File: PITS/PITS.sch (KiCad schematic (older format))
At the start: 47 parts, among them P1 CONN_02X20, P10 I2C, P11 I2C, P12 I2C, P13 I2C, P14 BATT, P2 BNC, P3 BNC, P4 BNC, P5 BNC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

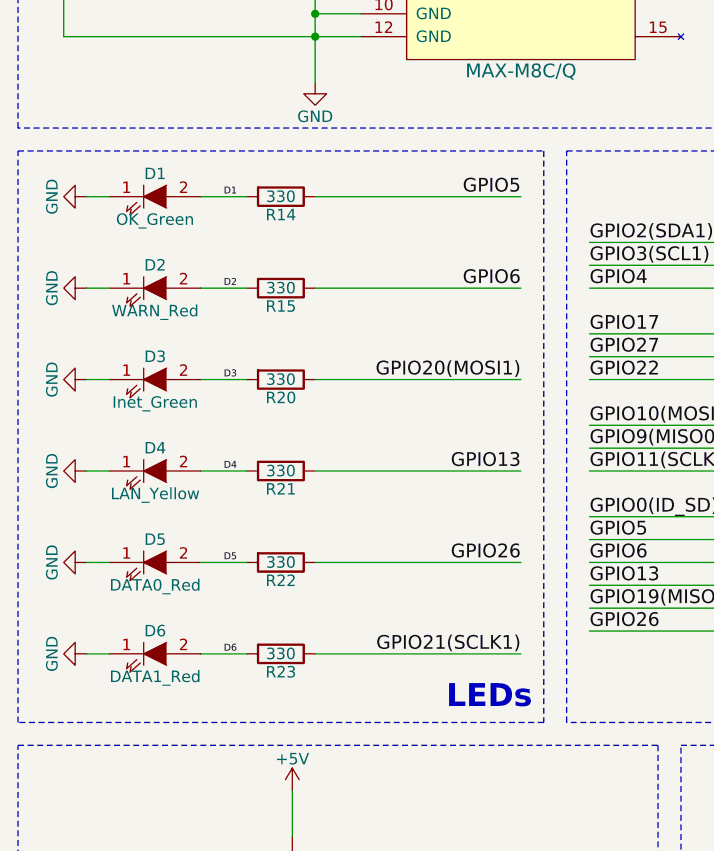
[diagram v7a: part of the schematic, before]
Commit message: layout - work in progress - first digital nets
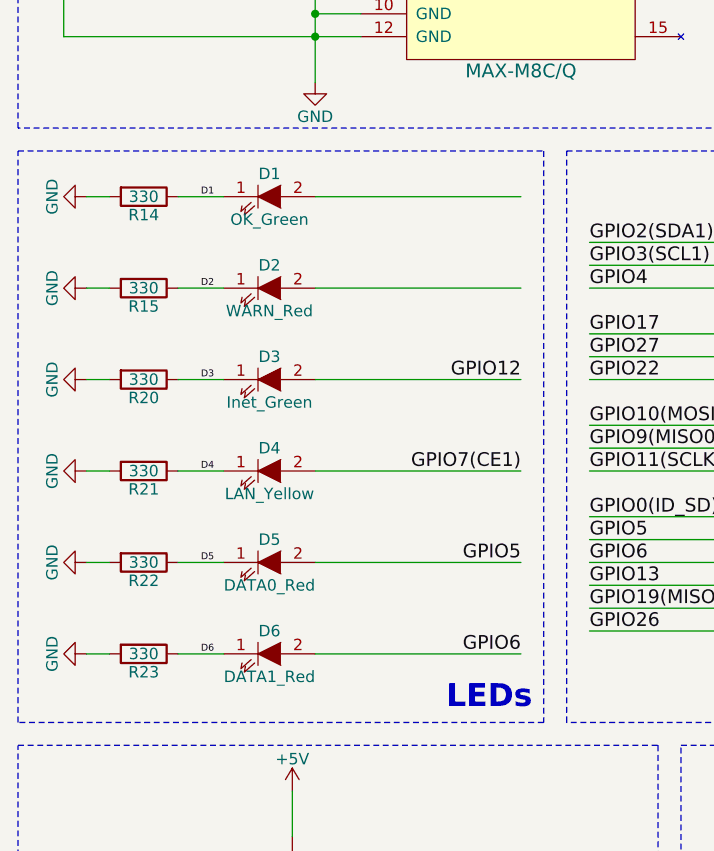
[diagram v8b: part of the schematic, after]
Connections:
- net D1: now also D1.1 (K), R14.1; no longer D1.2 (A), R14.2
- net D2: now also D2.1 (K), R15.1; no longer D2.2 (A), R15.2
- net D3: now also D3.1 (K), R20.1; no longer D3.2 (A), R20.2
- net D4: now also D4.1 (K), R21.1; no longer D4.2 (A), R21.2
- net D5: now also D5.1 (K), R22.1; no longer D5.2 (A), R22.2
- net D6: now also D6.1 (K), R23.1; no longer D6.2 (A), R23.2
- net GND: now also R14.2, R15.2, R20.2, R21.2, R22.2, R23.2; no longer D1.1 (K), D2.1 (K), D3.1 (K), D4.1 (K), D5.1 (K), D6.1 (K)
- net GPIO12: now also D3.2 (A)
- net GPIO13: no longer R21.1
- net GPIO20(MOSI1): no longer R20.1
- net GPIO21(SCLK1): no longer R23.1
- net GPIO26: no longer R22.1
- net GPIO5: now also D5.2 (A); no longer R14.1
- net GPIO6: now also D6.2 (A); no longer R15.1
- net GPIO7(CE1): now also D4.2 (A)
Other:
- moved on the sheet: D1, D2, D3, D4, D5, D6, R14, R15, R20, R21, R22, R23
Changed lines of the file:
@@
 L LED D1
 U 1 1 58198207
-P 1200 2900
-F 0 "D1" H 1200 3000 50  0000 C CNN
-F 1 "OK_Green" H 1200 2800 50  0000 C CNN
-F 2 "LEDs:LED_0603" H 1200 2900 50  0001 C CNN
-F 3 "" H 1200 2900 50  0000 C CNN
-	1    1200 2900
+P 1700 2900
+F 0 "D1" H 1700 3000 50  0000 C CNN
+F 1 "OK_Green" H 1700 2800 50  0000 C CNN
+F 2 "LEDs:LED_0603" H 1700 2900 50  0001 C CNN
+F 3 "" H 1700 2900 50  0000 C CNN
+	1    1700 2900
 	1    0    0    -1
 $EndComp
@@
 L LED D2
 U 1 1 5819820E
-P 1200 3300
-F 0 "D2" H 1200 3400 50  0000 C CNN
-F 1 "WARN_Red" H 1200 3200 50  0000 C CNN
-F 2 "LEDs:LED_0603" H 1200 3300 50  0001 C CNN
-F 3 "" H 1200 3300 50  0000 C CNN
-	1    1200 3300
+P 1700 3300
+F 0 "D2" H 1700 3400 50  0000 C CNN
+F 1 "WARN_Red" H 1700 3200 50  0000 C CNN
+F 2 "LEDs:LED_0603" H 1700 3300 50  0001 C CNN
+F 3 "" H 1700 3300 50  0000 C CNN
+	1    1700 3300
 	1    0    0    -1
 $EndComp
@@
 L LED D3
 U 1 1 58198215
-P 1200 3700
-F 0 "D3" H 1200 3800 50  0000 C CNN
-F 1 "Inet_Green" H 1200 3600 50  0000 C CNN
-F 2 "LEDs:LED_0603" H 1200 3700 50  0001 C CNN
-F 3 "" H 1200 3700 50  0000 C CNN
-	1    1200 3700
+P 1700 3700
+F 0 "D3" H 1700 3800 50  0000 C CNN
+F 1 "Inet_Green" H 1700 3600 50  0000 C CNN
+F 2 "LEDs:LED_0603" H 1700 3700 50  0001 C CNN
+F 3 "" H 1700 3700 50  0000 C CNN
+	1    1700 3700
 	1    0    0    -1
 $EndComp
@@
 L R R14
 U 1 1 581983DD
-P 1750 2900
-F 0 "R14" V 1830 2900 50  0000 C CNN
-F 1 "330" V 1750 2900 50  0000 C CNN
-F 2 "Resistors_SMD:R_0603_HandSoldering" V 1680 2900 50  0001 C CNN
-F 3 "" H 1750 2900 50  0000 C CNN
-	1    1750 2900
+P 1150 2900
+F 0 "R14" V 1230 2900 50  0000 C CNN
+F 1 "330" V 1150 2900 50  0000 C CNN
+F 2 "Resistors_SMD:R_0603_HandSoldering" V 1080 2900 50  0001 C CNN
+F 3 "" H 1150 2900 50  0000 C CNN
+	1    1150 2900
 	0    1    1    0
 $EndComp
@@
 L R R15
 U 1 1 58198843
-P 1750 3300
-F 0 "R15" V 1830 3300 50  0000 C CNN
-F 1 "330" V 1750 3300 50  0000 C CNN
-F 2 "Resistors_SMD:R_0603_HandSoldering" V 1680 3300 50  0001 C CNN
-F 3 "" H 1750 3300 50  0000 C CNN
-	1    1750 3300
+P 1150 3300
+F 0 "R15" V 1230 3300 50  0000 C CNN
+F 1 "330" V 1150 3300 50  0000 C CNN
+F 2 "Resistors_SMD:R_0603_HandSoldering" V 1080 3300 50  0001 C CNN
+F 3 "" H 1150 3300 50  0000 C CNN
+	1    1150 3300
 	0    1    1    0
 $EndComp
@@
 L R R20
 U 1 1 581988DE
-P 1750 3700
-F 0 "R20" V 1830 3700 50  0000 C CNN
-F 1 "330" V 1750 3700 50  0000 C CNN
-F 2 "Resistors_SMD:R_0603_HandSoldering" V 1680 3700 50  0001 C CNN
-F 3 "" H 1750 3700 50  0000 C CNN
-	1    1750 3700
+P 1150 3700
+F 0 "R20" V 1230 3700 50  0000 C CNN
+F 1 "330" V 1150 3700 50  0000 C CNN
+F 2 "Resistors_SMD:R_0603_HandSoldering" V 1080 3700 50  0001 C CNN
+F 3 "" H 1150 3700 50  0000 C CNN
+	1    1150 3700
 	0    1    1    0
 $EndComp
@@
 L LED D4
 U 1 1 5819A39B
-P 1200 4100
-F 0 "D4" H 1200 4200 50  0000 C CNN
-F 1 "LAN_Yellow" H 1200 4000 50  0000 C CNN
-F 2 "LEDs:LED_0603" H 1200 4100 50  0001 C CNN
-F 3 "" H 1200 4100 50  0000 C CNN
-	1    1200 4100
+P 1700 4100
+F 0 "D4" H 1700 4200 50  0000 C CNN
+F 1 "LAN_Yellow" H 1700 4000 50  0000 C CNN
+F 2 "LEDs:LED_0603" H 1700 4100 50  0001 C CNN
+F 3 "" H 1700 4100 50  0000 C CNN
+	1    1700 4100
 	1    0    0    -1
 $EndComp
@@
 L LED D5
 U 1 1 5819A3A2
-P 1200 4500
-F 0 "D5" H 1200 4600 50  0000 C CNN
-F 1 "DATA0_Red" H 1200 4400 50  0000 C CNN
-F 2 "LEDs:LED_0603" H 1200 4500 50  0001 C CNN
-F 3 "" H 1200 4500 50  0000 C CNN
-	1    1200 4500
+P 1700 4500
+F 0 "D5" H 1700 4600 50  0000 C CNN
+F 1 "DATA0_Red" H 1700 4400 50  0000 C CNN
+F 2 "LEDs:LED_0603" H 1700 4500 50  0001 C CNN
+F 3 "" H 1700 4500 50  0000 C CNN
+	1    1700 4500
 	1    0    0    -1
 $EndComp
@@
 L LED D6
 U 1 1 5819A3A9
-P 1200 4900
-F 0 "D6" H 1200 5000 50  0000 C CNN
-F 1 "DATA1_Red" H 1200 4800 50  0000 C CNN
-F 2 "LEDs:LED_0603" H 1200 4900 50  0001 C CNN
-F 3 "" H 1200 4900 50  0000 C CNN
-	1    1200 4900
+P 1700 4900
+F 0 "D6" H 1700 5000 50  0000 C CNN
+F 1 "DATA1_Red" H 1700 4800 50  0000 C CNN
+F 2 "LEDs:LED_0603" H 1700 4900 50  0001 C CNN
+F 3 "" H 1700 4900 50  0000 C CNN
+	1    1700 4900
 	1    0    0    -1
 $EndComp
@@
 L R R21
 U 1 1 5819A3B0
-P 1750 4100
-F 0 "R21" V 1830 4100 50  0000 C CNN
-F 1 "330" V 1750 4100 50  0000 C CNN
-F 2 "Resistors_SMD:R_0603_HandSoldering" V 1680 4100 50  0001 C CNN
-F 3 "" H 1750 4100 50  0000 C CNN
-	1    1750 4100
+P 1150 4100
+F 0 "R21" V 1230 4100 50  0000 C CNN
+F 1 "330" V 1150 4100 50  0000 C CNN
+F 2 "Resistors_SMD:R_0603_HandSoldering" V 1080 4100 50  0001 C CNN
+F 3 "" H 1150 4100 50  0000 C CNN
+	1    1150 4100
 	0    1    1    0
 $EndComp
@@
 L R R22
 U 1 1 5819A3B7
-P 1750 4500
-F 0 "R22" V 1830 4500 50  0000 C CNN
-F 1 "330" V 1750 4500 50  0000 C CNN
-F 2 "Resistors_SMD:R_0603_HandSoldering" V 1680 4500 50  0001 C CNN
-F 3 "" H 1750 4500 50  0000 C CNN
-	1    1750 4500
+P 1150 4500
+F 0 "R22" V 1230 4500 50  0000 C CNN
+F 1 "330" V 1150 4500 50  0000 C CNN
+F 2 "Resistors_SMD:R_0603_HandSoldering" V 1080 4500 50  0001 C CNN
+F 3 "" H 1150 4500 50  0000 C CNN
+	1    1150 4500
 	0    1    1    0
 $EndComp
@@
 L R R23
 U 1 1 5819A3BE
-P 1750 4900
-F 0 "R23" V 1830 4900 50  0000 C CNN
-F 1 "330" V 1750 4900 50  0000 C CNN
-F 2 "Resistors_SMD:R_0603_HandSoldering" V 1680 4900 50  0001 C CNN
-F 3 "" H 1750 4900 50  0000 C CNN
-	1    1750 4900
+P 1150 4900
+F 0 "R23" V 1230 4900 50  0000 C CNN
+F 1 "330" V 1150 4900 50  0000 C CNN
+F 2 "Resistors_SMD:R_0603_HandSoldering" V 1080 4900 50  0001 C CNN
+F 3 "" H 1150 4900 50  0000 C CNN
+	1    1150 4900
 	0    1    1    0
 $EndComp
@@
 	0    1    1    0
 $EndComp
-Text Label 2800 4500 2    60   ~ 0
-GPIO26
 Text Label 4300 1300 2    60   ~ 0
 GPIO19(MISO1)
-Text Label 2800 4100 2    60   ~ 0
-GPIO13
-Text Label 2800 3300 2    60   ~ 0
+Text Label 2800 4900 2    60   ~ 0
 GPIO6
-Text Label 2800 2900 2    60   ~ 0
+Text Label 2800 4500 2    60   ~ 0
 GPIO5
-Text Label 2800 4900 2    60   ~ 0
-GPIO21(SCLK1)
 Text Label 9800 4100 2    60   ~ 0
 GPIO2(SDA1)
@@
 Connection ~ 4000 4200
 Wire Wire Line
-	1400 2900 1600 2900
-Wire Wire Line
-	1600 3300 1400 3300
-Wire Wire Line
-	1400 3700 1600 3700
+	1300 2900 1500 2900
+Wire Wire Line
+	1500 3300 1300 3300
+Wire Wire Line
+	1300 3700 1500 3700
 Wire Wire Line
 	900  2900 1000 2900
@@
 	900  3700 1000 3700
 Wire Wire Line
-	1400 4100 1600 4100
-Wire Wire Line
-	1600 4500 1400 4500
-Wire Wire Line
-	1400 4900 1600 4900
+	1300 4100 1500 4100
+Wire Wire Line
+	1500 4500 1300 4500
+Wire Wire Line
+	1300 4900 1500 4900
 Wire Wire Line
 	900  4100 1000 4100
@@
 Text Label 4300 1400 2    60   ~ 0
 GPIO16(CE2)
-Text Label 2800 3700 2    60   ~ 0
-GPIO20(MOSI1)
 Text Label 4100 1600 2    60   ~ 0
 GPIO12
@@
 Text Label 2500 6100 0    30   ~ 0
 HX1-TXD
-Text Label 1500 2900 0    30   ~ 0
+Text Label 1400 2900 0    30   ~ 0
 D1
-Text Label 1500 3300 0    30   ~ 0
+Text Label 1400 3300 0    30   ~ 0
 D2
-Text Label 1500 3700 0    30   ~ 0
+Text Label 1400 3700 0    30   ~ 0
 D3
-Text Label 1500 4100 0    30   ~ 0
+Text Label 1400 4100 0    30   ~ 0
 D4
-Text Label 1500 4500 0    30   ~ 0
+Text Label 1400 4500 0    30   ~ 0
 D5
-Text Label 1500 4900 0    30   ~ 0
+Text Label 1400 4900 0    30   ~ 0
 D6
 $Comp
@@
 	1    0    0    -1
 $EndComp
+Text Label 2800 3700 2    60   ~ 0
+GPIO12
+Text Label 2800 4100 2    60   ~ 0
+GPIO7(CE1)
 $EndSCHEMATC
